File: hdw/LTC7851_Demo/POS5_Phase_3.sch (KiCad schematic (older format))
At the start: 0 parts

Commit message: Duplicated master phase, added status LEDs and a few test points
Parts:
- added C? (x2): 1uF, symbol Custom_Library:C_Custom
- added C? (x2): 0.1uF, symbol Custom_Library:C_Custom
- added C?: 0.22uF, symbol Custom_Library:C_Custom
- added C? (x2): 22uF, symbol Custom_Library:C_Custom
- added C? (x2): 100uF, symbol Custom_Library:C_Custom
- added C? (x6): 100uF, symbol Custom_Library:CP_Tant_Custom
- added L?: 0.47uH, symbol Custom_Library:L_Custom
- added R? (x2): 2, symbol Custom_Library:R_Custom
- added R?: 1.4k, symbol Custom_Library:R_Custom
- added TP? (x2): TP, symbol Custom_Library:TP
- added U?: SiC779, symbol Custom_Library:SiC779
- added U?: LTC7851UHH, symbol Custom_Library:LTC7851UHH
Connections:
- net labels added: +12V, +5.5V_MNG, +5V, GND, POS5_COMP, POS5_EXTVCC, POS5_IAVG, POS5_ILIM, POS5_ISNS1_+, POS5_ISNS1_-, POS5_PGOOD_OC, POS5_RUN, POS5_SMOD, POS5_SS, POS5_VOSNS, ~POS5_THDN
- wire segments 0 -> 110
- no-connect marks 0 -> 2
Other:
- note added: "Remove bulk caps from onsheet when bringing into project"
- note added: "Route as diff pair"

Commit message: Assigned some custom footprints
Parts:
- U?: footprint (none) -> Custom Footprints Library:MLP66-40_6x6mm_Pitch0.5mm
- U?: footprint (none) -> Custom Footprints Library:QFN-58-1EP_9x5mm_Pitch0.4mm
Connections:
- net labels added: POS5_ISNS3_+, POS5_ISNS3_-
- net labels removed: POS5_ISNS1_+, POS5_ISNS1_-
- wire segments 110 -> 112
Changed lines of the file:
@@
 F 0 "U?" H 6080 960 50  0000 C CNN
 F 1 "SiC779" H 6080 4660 50  0000 C CNN
-F 2 "" H 4430 3560 50  0001 C CNN
+F 2 "Custom Footprints Library:MLP66-40_6x6mm_Pitch0.5mm" H 4430 3560 50  0001 C CNN
 F 3 "http://www.vishay.com/docs/67538/sic779.pdf" H 6080 2810 50  0001 C CNN
 F 4 "SIC779CD-T1-GE3CT-ND" H 6080 2810 50  0001 C CNN "Digi-Key PN"
@@
 F 0 "U?" H 2910 2160 50  0000 R CNN
 F 1 "LTC7851UHH" H 2510 6260 50  0000 C CNN
-F 2 "" H -140 4910 50  0001 C CNN
+F 2 "Custom Footprints Library:QFN-58-1EP_9x5mm_Pitch0.4mm" H -140 4910 50  0001 C CNN
 F 3 "http://www.analog.com/media/en/technical-documentation/data-sheets/LTC7851.pdf" H 2510 4210 50  0001 C CNN
 F 4 "LTC7851IUHH#PBF-ND" H 2510 4210 50  0001 C CNN "Digi-Key PN"
@@
 POS5_RUN
 Text Label 3160 3310 0    50   ~ 0
-POS5_ISNS1_+
+POS5_ISNS3_+
 Text Label 3160 3410 0    50   ~ 0
-POS5_ISNS1_-
+POS5_ISNS3_-
 Text Notes 3270 3670 0    50   ~ 0
 Route as diff pair
@@
 Text GLabel 3060 5110 2    50   UnSpc ~ 0
 POS5_EXTVCC
+Wire Wire Line
+	6730 4110 6810 4110
+Wire Wire Line
+	6810 4110 6810 4010
+Connection ~ 6810 4010
 $EndSCHEMATC

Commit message: Annotated schematic
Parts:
- gave numbers to parts that had none: 23

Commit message: Added Digi-Key part numbers for all parts
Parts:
- C604, C609: Digi-Key PN PN -> 1276-6524-1-ND
- C606, C608: Digi-Key PN PN -> 490-4779-1-ND
- C610: Digi-Key PN PN -> 490-5402-1-ND
- C612: Digi-Key PN PN -> 587-3432-1-ND
- R601, R602: Digi-Key PN PN -> RMCF0603FT2R00CT-ND
- R603: Digi-Key PN PN -> P1.40KHCT-ND
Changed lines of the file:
@@
 F 5 "16V" H 4410 1340 50  0000 R CNN "Voltage"
 F 6 "X7R" H 4410 1240 50  0000 R CNN "Dielectric"
-F 7 "PN" H 4985 1840 60  0001 C CNN "Digi-Key PN"
+F 7 "1276-6524-1-ND" H 4985 1840 60  0001 C CNN "Digi-Key PN"
 	1    4560 1340
 	1    0    0    -1
@@
 F 2 "" H 6980 2470 50  0001 C CNN
 F 3 "" H 6980 2470 50  0001 C CNN
-F 4 "PN" H 7280 2870 60  0001 C CNN "Digi-Key PN"
+F 4 "RMCF0603FT2R00CT-ND" H 7280 2870 60  0001 C CNN "Digi-Key PN"
 F 5 "0603" H 7080 2550 50  0000 L CNN "display_footprint"
 F 6 "1%" H 7080 2470 50  0000 L CNN "Tolerance"
@@
 F 5 "50V" H 6830 2850 50  0000 R CNN "Voltage"
 F 6 "X7R" H 6830 2750 50  0000 R CNN "Dielectric"
-F 7 "PN" H 7405 3350 60  0001 C CNN "Digi-Key PN"
+F 7 "490-4779-1-ND" H 7405 3350 60  0001 C CNN "Digi-Key PN"
 	1    6980 2850
 	1    0    0    -1
@@
 F 2 "" H 7190 3770 50  0001 C CNN
 F 3 "" H 7190 3770 50  0001 C CNN
-F 4 "PN" H 7490 4170 60  0001 C CNN "Digi-Key PN"
+F 4 "P1.40KHCT-ND" H 7490 4170 60  0001 C CNN "Digi-Key PN"
 F 5 "0603" H 7290 3850 50  0000 L CNN "display_footprint"
 F 6 "1%" H 7290 3770 50  0000 L CNN "Tolerance"
@@
 F 2 "" H 7478 3890 50  0001 C CNN
 F 3 "" H 7465 4140 50  0001 C CNN
-F 4 "PN" H 7865 4540 60  0001 C CNN "Digi-Key PN"
+F 4 "490-5402-1-ND" H 7865 4540 60  0001 C CNN "Digi-Key PN"
 F 5 "0603" V 7098 4040 50  0000 C CNN "display_footprint"
 F 6 "50V" V 7189 4040 50  0000 C CNN "Voltage"
@@
 F 5 "10V" H 8270 3540 50  0000 R CNN "Voltage"
 F 6 "X5R" H 8270 3440 50  0000 R CNN "Dielectric"
-F 7 "PN" H 8845 4040 60  0001 C CNN "Digi-Key PN"
+F 7 "587-3432-1-ND" H 8845 4040 60  0001 C CNN "Digi-Key PN"
 	1    8420 3540
 	1    0    0    -1
@@
 F 5 "50V" H 5030 1870 50  0000 R CNN "Voltage"
 F 6 "X7R" H 5030 1770 50  0000 R CNN "Dielectric"
-F 7 "PN" H 5605 2370 60  0001 C CNN "Digi-Key PN"
+F 7 "490-4779-1-ND" H 5605 2370 60  0001 C CNN "Digi-Key PN"
 	1    5180 1870
 	1    0    0    -1
@@
 F 2 "" H 5180 1340 50  0001 C CNN
 F 3 "" H 5180 1340 50  0001 C CNN
-F 4 "PN" H 5480 1740 60  0001 C CNN "Digi-Key PN"
+F 4 "RMCF0603FT2R00CT-ND" H 5480 1740 60  0001 C CNN "Digi-Key PN"
 F 5 "0603" H 5280 1420 50  0000 L CNN "display_footprint"
 F 6 "1%" H 5280 1340 50  0000 L CNN "Tolerance"
@@
 F 5 "16V" H 7130 1340 50  0000 R CNN "Voltage"
 F 6 "X7R" H 7130 1240 50  0000 R CNN "Dielectric"
-F 7 "PN" H 7705 1840 60  0001 C CNN "Digi-Key PN"
+F 7 "1276-6524-1-ND" H 7705 1840 60  0001 C CNN "Digi-Key PN"
 	1    7280 1340
 	1    0    0    -1

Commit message: Assigned footprints
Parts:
- C601, C602, C603, C605, C607, C615: footprint (none) -> Capacitors_Tantalum_SMD:CP_Tantalum_Case-B_EIA-3528-21_Reflow
- C604, C606, C608, C609, C610: footprint (none) -> Capacitors_SMD:C_0603
- C611, C612, C613, C614: footprint (none) -> Capacitors_SMD:C_1210
- L601: footprint (none) -> Inductors_SMD:L_Vishay_IHLP-4040
- R601, R602, R603: footprint (none) -> Resistors_SMD:R_0603
- TP601, TP602: footprint (none) -> Measurement_Points:Measurement_Point_Round-SMD-Pad_Small
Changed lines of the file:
@@
 F 0 "C604" H 4585 1440 50  0000 L CNN
 F 1 "1uF" H 4585 1240 50  0000 L CNN
-F 2 "" H 4598 1190 50  0001 C CNN
+F 2 "Capacitors_SMD:C_0603" H 4598 1190 50  0001 C CNN
 F 3 "" H 4585 1440 50  0001 C CNN
 F 4 "0603" H 4410 1440 50  0000 R CNN "display_footprint"
@@
 F 0 "TP601" V 5430 2960 50  0000 L CNN
 F 1 "TP" H 5430 2960 50  0001 C CNN
-F 2 "" H 5430 2810 60  0000 C CNN
+F 2 "Measurement_Points:Measurement_Point_Round-SMD-Pad_Small" H 5430 2810 60  0001 C CNN
 F 3 "" H 5430 2810 60  0000 C CNN
 	1    5430 2810
@@
 F 0 "TP602" V 5430 3060 50  0000 L CNN
 F 1 "TP" H 5430 3060 50  0001 C CNN
-F 2 "" H 5430 2910 60  0000 C CNN
+F 2 "Measurement_Points:Measurement_Point_Round-SMD-Pad_Small" H 5430 2910 60  0001 C CNN
 F 3 "" H 5430 2910 60  0000 C CNN
 	1    5430 2910
@@
 F 0 "L601" V 7390 3310 50  0000 C CNN
 F 1 "0.47uH" V 7515 3310 50  0000 C CNN
-F 2 "" H 7440 3310 50  0001 C CNN
+F 2 "Inductors_SMD:L_Vishay_IHLP-4040" H 7440 3310 50  0001 C CNN
 F 3 "" H 7440 3310 50  0001 C CNN
 F 4 "541-2595-1-ND" H 7440 3310 50  0001 C CNN "Digi-Key PN"
@@
 F 0 "R602" H 6880 2470 50  0000 R CNN
 F 1 "2" V 6980 2470 50  0000 C CNN
-F 2 "" H 6980 2470 50  0001 C CNN
+F 2 "Resistors_SMD:R_0603" H 6980 2470 50  0001 C CNN
 F 3 "" H 6980 2470 50  0001 C CNN
 F 4 "RMCF0603FT2R00CT-ND" H 7280 2870 60  0001 C CNN "Digi-Key PN"
@@
 F 0 "C608" H 7005 2950 50  0000 L CNN
 F 1 "0.1uF" H 7005 2750 50  0000 L CNN
-F 2 "" H 7018 2700 50  0001 C CNN
+F 2 "Capacitors_SMD:C_0603" H 7018 2700 50  0001 C CNN
 F 3 "" H 7005 2950 50  0001 C CNN
 F 4 "0603" H 6830 2950 50  0000 R CNN "display_footprint"
@@
 F 0 "R603" H 7290 3920 50  0000 L CNN
 F 1 "1.4k" V 7190 3770 40  0000 C CNN
-F 2 "" H 7190 3770 50  0001 C CNN
+F 2 "Resistors_SMD:R_0603" H 7190 3770 50  0001 C CNN
 F 3 "" H 7190 3770 50  0001 C CNN
 F 4 "P1.40KHCT-ND" H 7490 4170 60  0001 C CNN "Digi-Key PN"
@@
 F 0 "C610" V 6916 4040 50  0000 C CNN
 F 1 "0.22uF" V 7007 3910 50  0000 L CNN
-F 2 "" H 7478 3890 50  0001 C CNN
+F 2 "Capacitors_SMD:C_0603" H 7478 3890 50  0001 C CNN
 F 3 "" H 7465 4140 50  0001 C CNN
 F 4 "490-5402-1-ND" H 7865 4540 60  0001 C CNN "Digi-Key PN"
@@
 F 0 "C611" H 7905 1440 50  0000 L CNN
 F 1 "22uF" H 7905 1240 50  0000 L CNN
-F 2 "" H 7918 1190 50  0001 C CNN
+F 2 "Capacitors_SMD:C_1210" H 7918 1190 50  0001 C CNN
 F 3 "" H 7905 1440 50  0001 C CNN
 F 4 "445-1436-1-ND" H 8305 1840 60  0001 C CNN "Digi-Key PN"
@@
 F 0 "C612" H 8445 3640 50  0000 L CNN
 F 1 "100uF" H 8445 3440 50  0000 L CNN
-F 2 "" H 8458 3390 50  0001 C CNN
+F 2 "Capacitors_SMD:C_1210" H 8458 3390 50  0001 C CNN
 F 3 "" H 8445 3640 50  0001 C CNN
 F 4 "1210" H 8270 3640 50  0000 R CNN "display_footprint"
@@
 F 0 "C606" H 5205 1970 50  0000 L CNN
 F 1 "0.1uF" H 5205 1770 50  0000 L CNN
-F 2 "" H 5218 1720 50  0001 C CNN
+F 2 "Capacitors_SMD:C_0603" H 5218 1720 50  0001 C CNN
 F 3 "" H 5205 1970 50  0001 C CNN
 F 4 "0603" H 5030 1970 50  0000 R CNN "display_footprint"
@@
 F 0 "R601" H 5080 1340 50  0000 R CNN
 F 1 "2" V 5180 1340 50  0000 C CNN
-F 2 "" H 5180 1340 50  0001 C CNN
+F 2 "Resistors_SMD:R_0603" H 5180 1340 50  0001 C CNN
 F 3 "" H 5180 1340 50  0001 C CNN
 F 4 "RMCF0603FT2R00CT-ND" H 5480 1740 60  0001 C CNN "Digi-Key PN"
@@
 F 0 "C609" H 7305 1440 50  0000 L CNN
 F 1 "1uF" H 7305 1240 50  0000 L CNN
-F 2 "" H 7318 1190 50  0001 C CNN
+F 2 "Capacitors_SMD:C_0603" H 7318 1190 50  0001 C CNN
 F 3 "" H 7305 1440 50  0001 C CNN
 F 4 "0603" H 7130 1440 50  0000 R CNN "display_footprint"
@@
 F 0 "C615" H 9645 3640 50  0000 L CNN
 F 1 "100uF" H 9645 3440 50  0000 L CNN
-F 2 "" H 9658 3390 50  0001 C CNN
+F 2 "Capacitors_Tantalum_SMD:CP_Tantalum_Case-B_EIA-3528-21_Reflow" H 9658 3390 50  0001 C CNN
 F 3 "" H 9645 3640 50  0001 C CNN
 F 4 "478-9994-1-ND" H 9620 3540 50  0001 C CNN "Digi-Key PN"
@@
 F 0 "C614" H 9045 3640 50  0000 L CNN
 F 1 "100uF" H 9045 3440 50  0000 L CNN
-F 2 "" H 9058 3390 50  0001 C CNN
+F 2 "Capacitors_SMD:C_1210" H 9058 3390 50  0001 C CNN
 F 3 "" H 9045 3640 50  0001 C CNN
 F 4 "587-3432-1-ND" H 9445 4040 60  0001 C CNN "Digi-Key PN"
@@
 F 0 "C613" H 8505 1440 50  0000 L CNN
 F 1 "22uF" H 8505 1240 50  0000 L CNN
-F 2 "" H 8518 1190 50  0001 C CNN
+F 2 "Capacitors_SMD:C_1210" H 8518 1190 50  0001 C CNN
 F 3 "" H 8505 1440 50  0001 C CNN
 F 4 "445-1436-1-ND" H 8905 1840 60  0001 C CNN "Digi-Key PN"
@@
 F 0 "C601" H 3355 7470 50  0000 L CNN
 F 1 "100uF" H 3355 7270 50  0000 L CNN
-F 2 "" H 3368 7220 50  0001 C CNN
+F 2 "Capacitors_Tantalum_SMD:CP_Tantalum_Case-B_EIA-3528-21_Reflow" H 3368 7220 50  0001 C CNN
 F 3 "" H 3355 7470 50  0001 C CNN
 F 4 "478-9994-1-ND" H 3330 7370 50  0001 C CNN "Digi-Key PN"
@@
 F 0 "C602" H 3955 7470 50  0000 L CNN
 F 1 "100uF" H 3955 7270 50  0000 L CNN
-F 2 "" H 3968 7220 50  0001 C CNN
+F 2 "Capacitors_Tantalum_SMD:CP_Tantalum_Case-B_EIA-3528-21_Reflow" H 3968 7220 50  0001 C CNN
 F 3 "" H 3955 7470 50  0001 C CNN
 F 4 "478-9994-1-ND" H 3930 7370 50  0001 C CNN "Digi-Key PN"
@@
 F 0 "C603" H 4555 7470 50  0000 L CNN
 F 1 "100uF" H 4555 7270 50  0000 L CNN
-F 2 "" H 4568 7220 50  0001 C CNN
+F 2 "Capacitors_Tantalum_SMD:CP_Tantalum_Case-B_EIA-3528-21_Reflow" H 4568 7220 50  0001 C CNN
 F 3 "" H 4555 7470 50  0001 C CNN
 F 4 "478-9994-1-ND" H 4530 7370 50  0001 C CNN "Digi-Key PN"
@@
 F 0 "C605" H 5155 7470 50  0000 L CNN
 F 1 "100uF" H 5155 7270 50  0000 L CNN
-F 2 "" H 5168 7220 50  0001 C CNN
+F 2 "Capacitors_Tantalum_SMD:CP_Tantalum_Case-B_EIA-3528-21_Reflow" H 5168 7220 50  0001 C CNN
 F 3 "" H 5155 7470 50  0001 C CNN
 F 4 "478-9994-1-ND" H 5130 7370 50  0001 C CNN "Digi-Key PN"
@@
 F 0 "C607" H 5755 7470 50  0000 L CNN
 F 1 "100uF" H 5755 7270 50  0000 L CNN
-F 2 "" H 5768 7220 50  0001 C CNN
+F 2 "Capacitors_Tantalum_SMD:CP_Tantalum_Case-B_EIA-3528-21_Reflow" H 5768 7220 50  0001 C CNN
 F 3 "" H 5755 7470 50  0001 C CNN
 F 4 "478-9994-1-ND" H 5730 7370 50  0001 C CNN "Digi-Key PN"

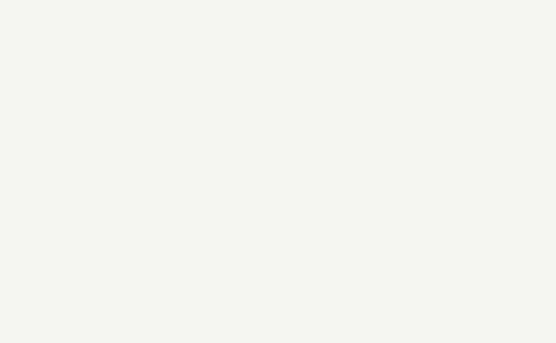
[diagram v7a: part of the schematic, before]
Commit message: Added page titles
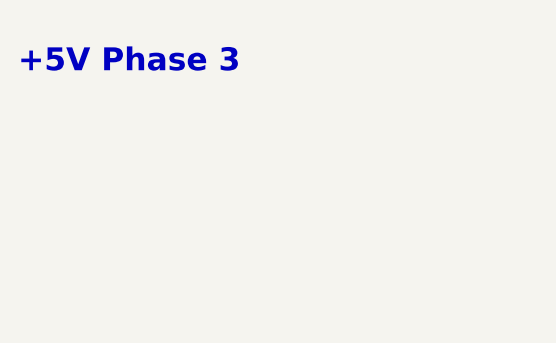
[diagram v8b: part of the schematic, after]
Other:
- note added: "+5V Phase 3"
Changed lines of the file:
@@
 	6810 4110 6810 4010
 Connection ~ 6810 4010
+Text Notes 540  690  0    100  ~ 20
++5V Phase 3
 $EndSCHEMATC
